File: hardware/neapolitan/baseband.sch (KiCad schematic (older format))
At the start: 136 parts, among them P14 XCVR_CLKOUT, P15 INTR, P16 CLKIN, P18 OEB, P2 CLKOUT, P36 VAA, P37 SCL, P38 SDA, P39 SSP1_SCK, P40 SSP1_MOSI, P41 SSP1_MISO, P53 CS_XCVR, P54 CS_AD, P55 TXENABLE, P56 RXENABLE, P57 XTAL2, P58 GCK1, P59 GCK2, P60 SGPIO_CLK, P61 DA0, P62 DA7, P63 DD0, P64 DD9, P65 DA4, P66 DD5, P67 RSSI, P83 GND, P84 GND, P85 GND, P86 GND, P87 GND, P88 GND, P89 GND, P9 BASEBAND, P90 GND, P91 GND, P92 GND, Q3 MOSFET_P, T3 RX_BALUN, T4 TX_BALUN, U17 MAX2837, U18 MAX5864, U19 SI5351C, X1 GSG-XTAL4PIN

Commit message: Neapolitan: deleted MCU and other things not needed
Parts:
- removed C100, C97, C98: 330nF, hackrf:GSG-0402, symbol C
- removed C101, C103, C107, C108, C109, C110, C95, C96: 22pF, hackrf:GSG-0402, symbol C
- removed C123, C71, C73, C75, C77, C79, C81, C83: 100nF, hackrf:GSG-0402, symbol C
- removed C124, C72, C74, C76, C78, C80, C82: 2.2uF, hackrf:GSG-0402, symbol C
- removed P54: CS_AD, hackrf:GSG-TESTPOINT-50MIL, symbol CONN_1
- removed P58: GCK1, hackrf:GSG-TESTPOINT-50MIL, symbol CONN_1
- removed P59: GCK2, hackrf:GSG-TESTPOINT-50MIL, symbol CONN_1
- removed P60: SGPIO_CLK, hackrf:GSG-TESTPOINT-50MIL, symbol CONN_1
- removed P61: DA0, hackrf:GSG-TESTPOINT-50MIL, symbol CONN_1
- removed P62: DA7, hackrf:GSG-TESTPOINT-50MIL, symbol CONN_1
- removed P63: DD0, hackrf:GSG-TESTPOINT-50MIL, symbol CONN_1
- removed P64: DD9, hackrf:GSG-TESTPOINT-50MIL, symbol CONN_1
- removed P65: DA4, hackrf:GSG-TESTPOINT-50MIL, symbol CONN_1
- removed P66: DD5, hackrf:GSG-TESTPOINT-50MIL, symbol CONN_1
- removed R10, R13, R8, R9: 1k, hackrf:GSG-0402, symbol R
- removed R14, R15, R16, R17: 4k7, hackrf:GSG-0402, symbol R
- removed R20, R21, R22, R23: 0, hackrf:GSG-0402, symbol R
- removed U18: MAX5864, hackrf:GSG-QFN48-7, symbol MAX5864
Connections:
- net labels removed: COM, CS_AD, DA0, DA1, DA2, DA3, DA4, DA5, DA6, DA7, DD0, DD1, DD2, DD3, DD4, DD5, DD6, DD7, DD8, DD9, IA+, IA-, ID+, ID-, QA+, QA-, QD+, QD-, REFN, REFP
- wire segments 320 -> 215
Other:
- note removed: "1%"

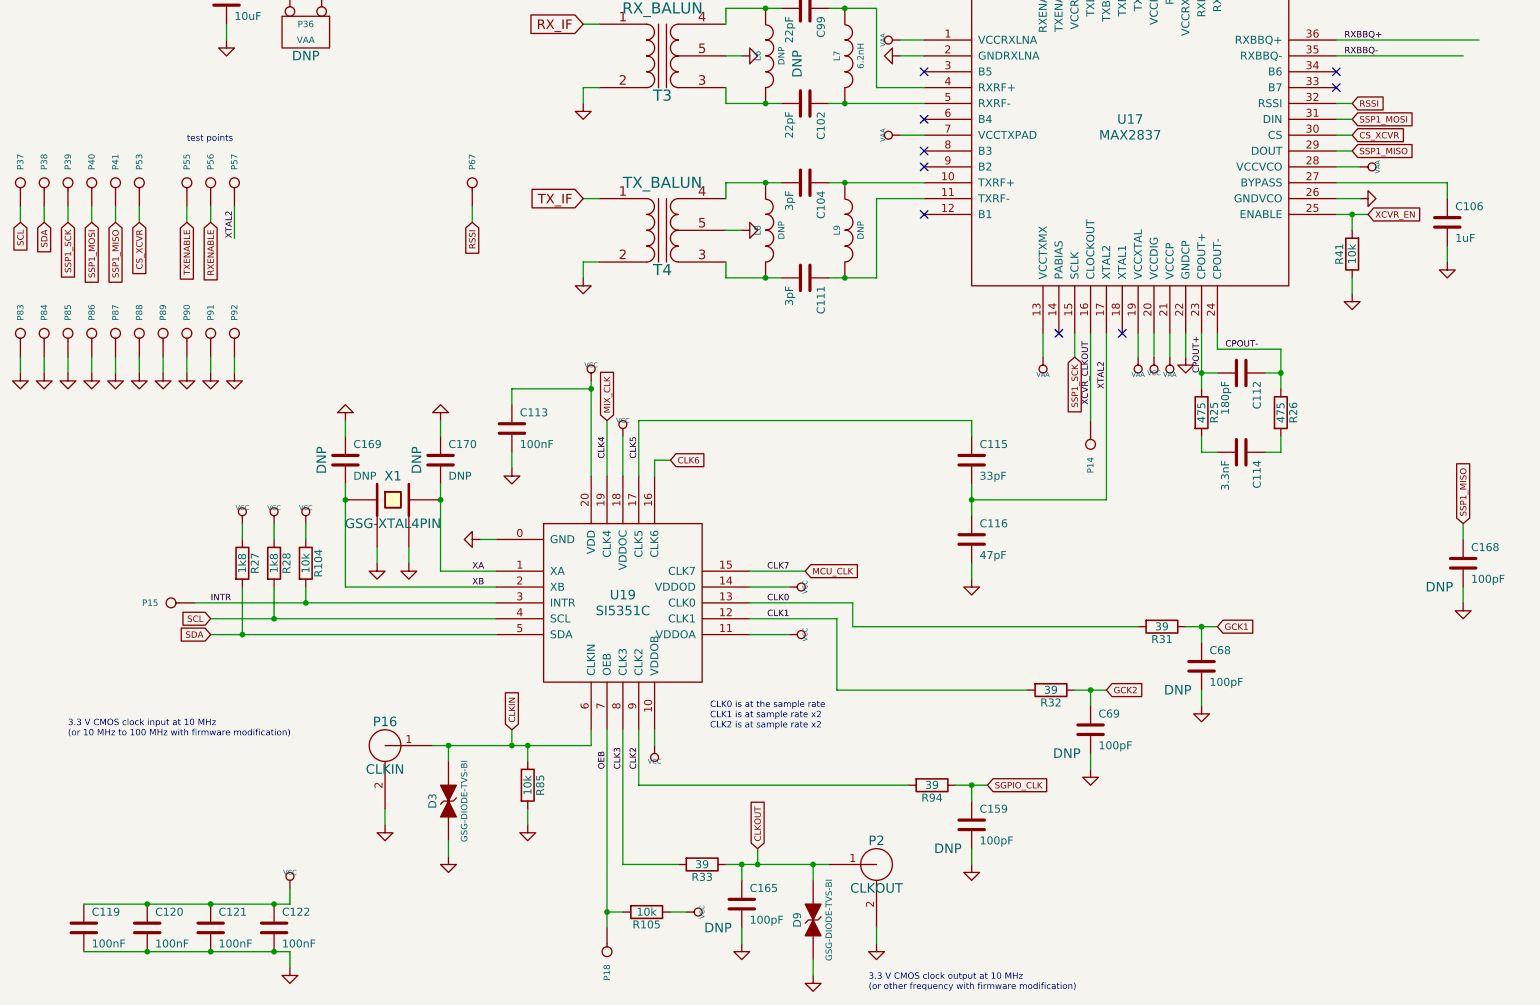
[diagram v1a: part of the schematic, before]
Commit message: Neapolitan: header pin assignments
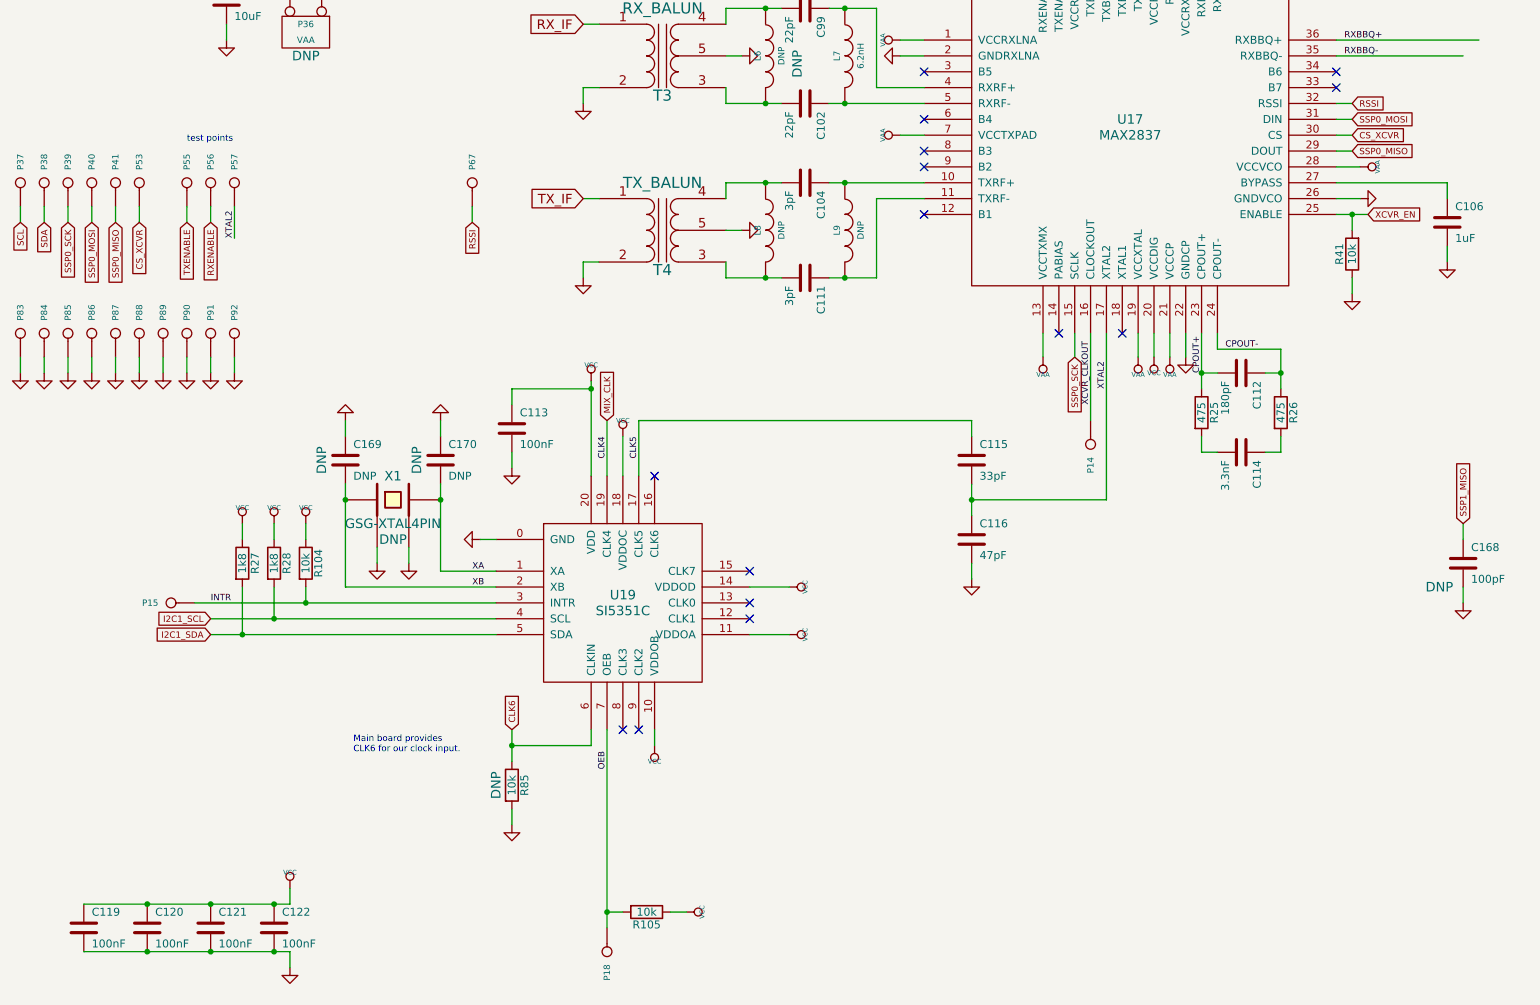
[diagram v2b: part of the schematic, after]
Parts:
- removed C159, C165, C68, C69: 100pF, hackrf:GSG-0402, symbol C
- removed D3, D9: GSG-DIODE-TVS-BI, hackrf:GSG-0402, symbol GSG-DIODE-TVS-BI
- removed P16: CLKIN, hackrf:GSG-SMA-73251-2120, symbol GSG-RF-CONN
- removed P2: CLKOUT, hackrf:GSG-SMA-73251-2120, symbol GSG-RF-CONN
- removed R31, R32, R33, R94: 39, hackrf:GSG-0402, symbol R
- P39: value SSP1_SCK -> SSP0_SCK
- P40: value SSP1_MOSI -> SSP0_MOSI
- P41: value SSP1_MISO -> SSP0_MISO
- R85, X1: Note (none) -> DNP
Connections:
- net labels added: I2C1_SCL, I2C1_SDA, SSP0_MISO, SSP0_MOSI, SSP0_SCK
- net labels removed: CLK0, CLK1, CLK2, CLK3, CLK7, CLKIN, CLKOUT, GCK1, GCK2, MCU_CLK, SGPIO_CLK, SSP1_MOSI, SSP1_SCK
- wire segments 215 -> 182
- no-connect marks 10 -> 16
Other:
- note added: "Main board provides\nCLK6 for our clock input."
- note removed: "3.3 V CMOS clock input at 10 MHz\n(or 10 MHz to 100 MHz with firmware modification)"
- note removed: "3.3 V CMOS clock output at 10 MHz\n(or other frequency with firmware modification)"
- note removed: "CLK0 is at the sample rate\nCLK1 is at sample rate x2\nCLK2 is at sample rate x2"
- moved on the sheet: R85

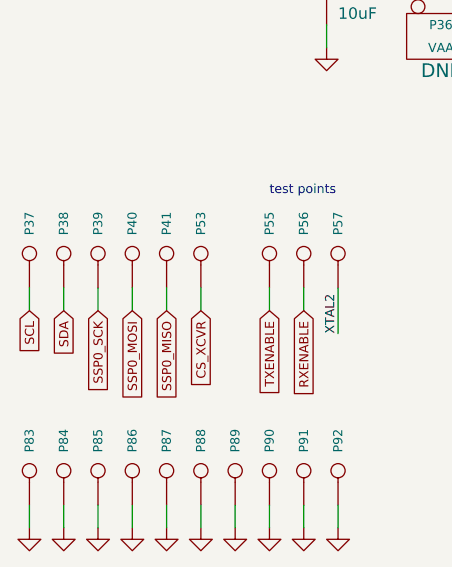
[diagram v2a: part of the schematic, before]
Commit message: Neapolitan: added I/O expander
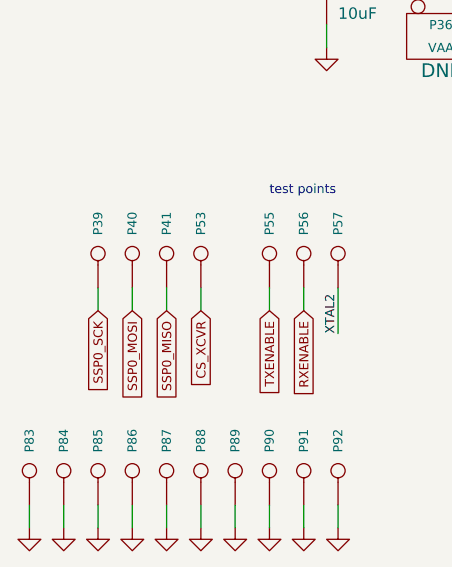
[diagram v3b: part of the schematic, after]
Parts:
- removed P37: SCL, hackrf:GSG-TESTPOINT-50MIL, symbol CONN_1
- removed P38: SDA, hackrf:GSG-TESTPOINT-50MIL, symbol CONN_1
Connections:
- net labels removed: SCL, SDA
- wire segments 182 -> 180
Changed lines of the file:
@@
 LIBS:valves
 LIBS:hackrf
+LIBS:gsg-symbols
 LIBS:neapolitan-cache
 EELAYER 25 0
@@
 F 4 "DNP" H 1000 5300 60  0001 C CNN "Note"
 	1    1000 5300
-	0    -1   -1   0
-$EndComp
-$Comp
-L CONN_1 P38
-U 1 1 5052A32D
-P 850 5300
-F 0 "P38" H 930 5300 40  0000 L CNN
-F 1 "SDA" H 850 5355 30  0001 C CNN
-F 2 "hackrf:GSG-TESTPOINT-50MIL" H 850 5300 60  0001 C CNN
-F 3 "" H 850 5300 60  0001 C CNN
-F 4 "DNP" H 850 5300 60  0001 C CNN "Note"
-	1    850  5300
-	0    -1   -1   0
-$EndComp
-Text GLabel 850  5550 3    40   Input ~ 0
-SDA
-Text GLabel 700  5550 3    40   Input ~ 0
-SCL
-$Comp
-L CONN_1 P37
-U 1 1 5052A309
-P 700 5300
-F 0 "P37" H 780 5300 40  0000 L CNN
-F 1 "SCL" H 700 5355 30  0001 C CNN
-F 2 "hackrf:GSG-TESTPOINT-50MIL" H 700 5300 60  0001 C CNN
-F 3 "" H 700 5300 60  0001 C CNN
-F 4 "DNP" H 700 5300 60  0001 C CNN "Note"
-	1    700  5300
 	0    -1   -1   0
 $EndComp
@@
 	1000 5450 1000 5550
 Wire Wire Line
-	850  5450 850  5550
-Wire Wire Line
-	700  5450 700  5550
-Wire Wire Line
 	2400 3900 2400 4000

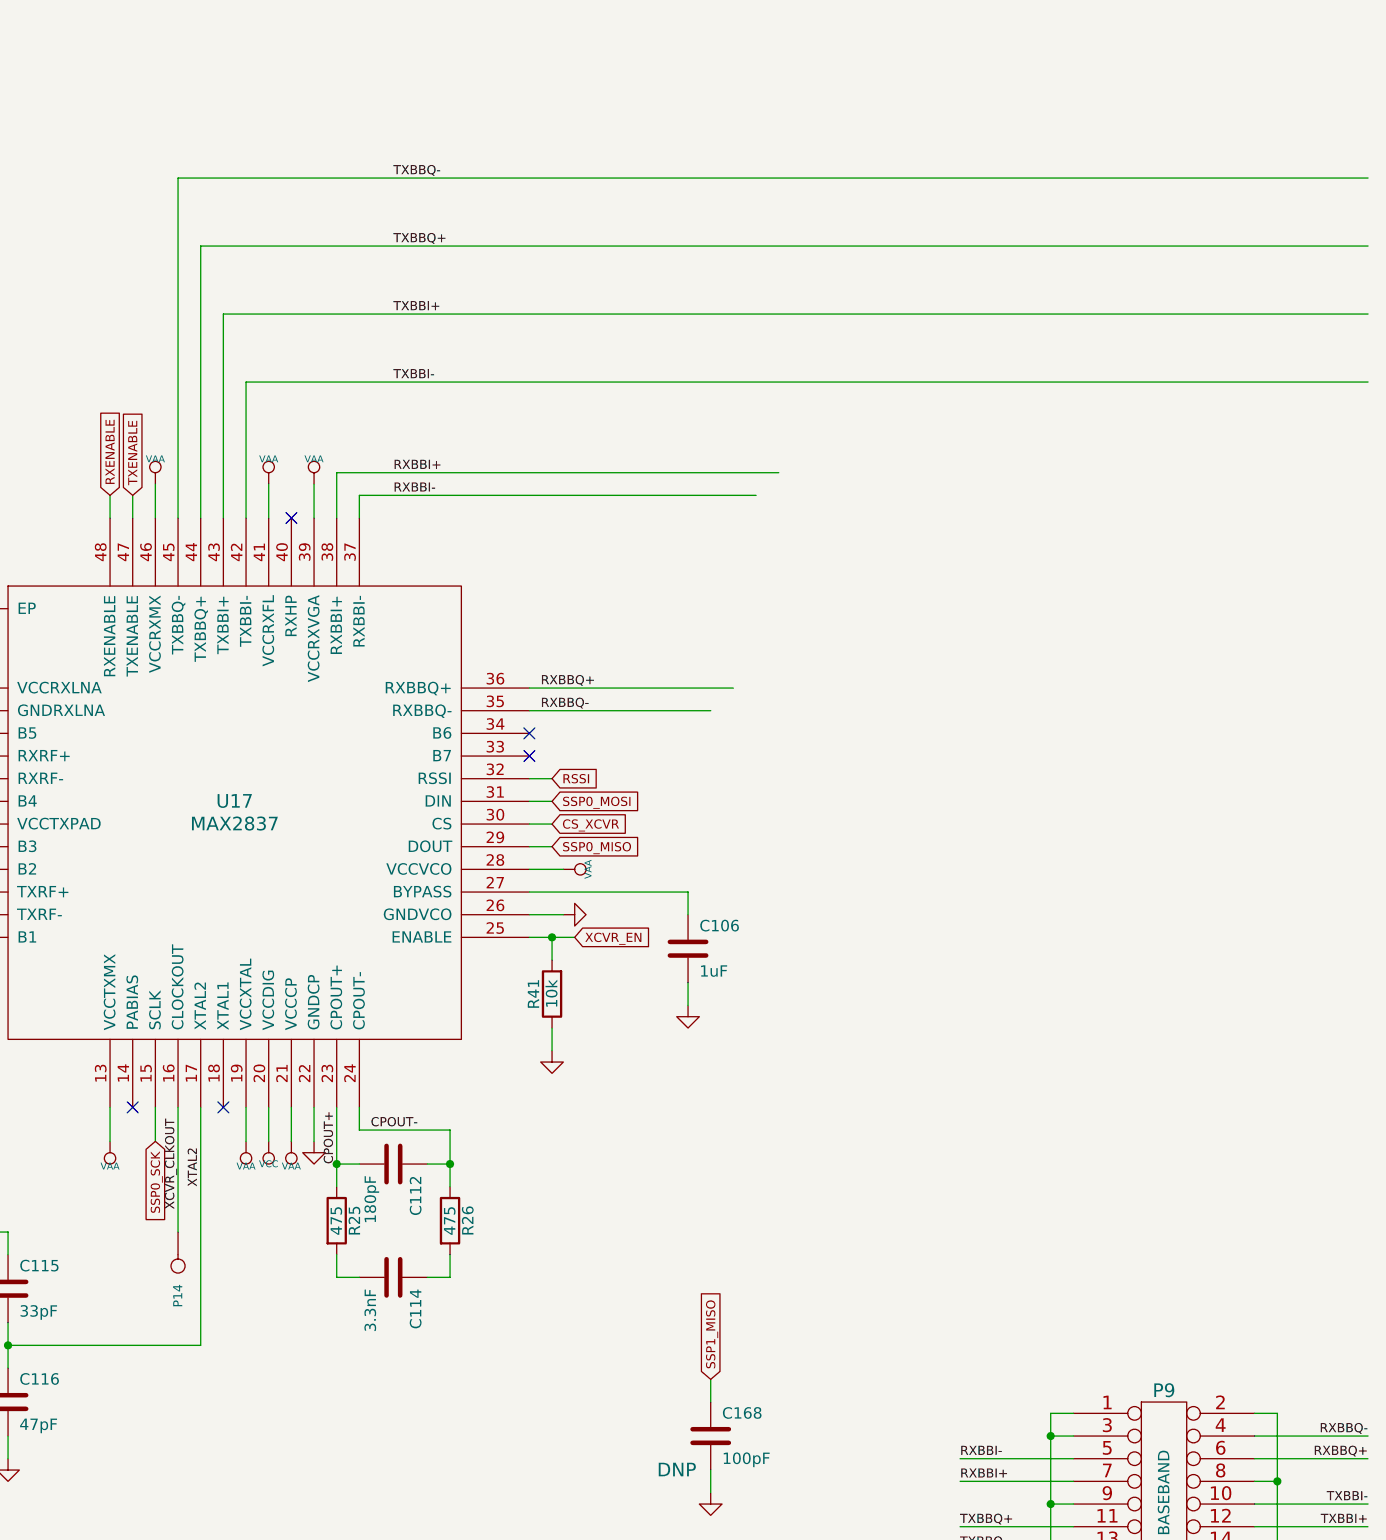
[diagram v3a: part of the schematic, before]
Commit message: Neapolitan: schematic annotation and cleanup
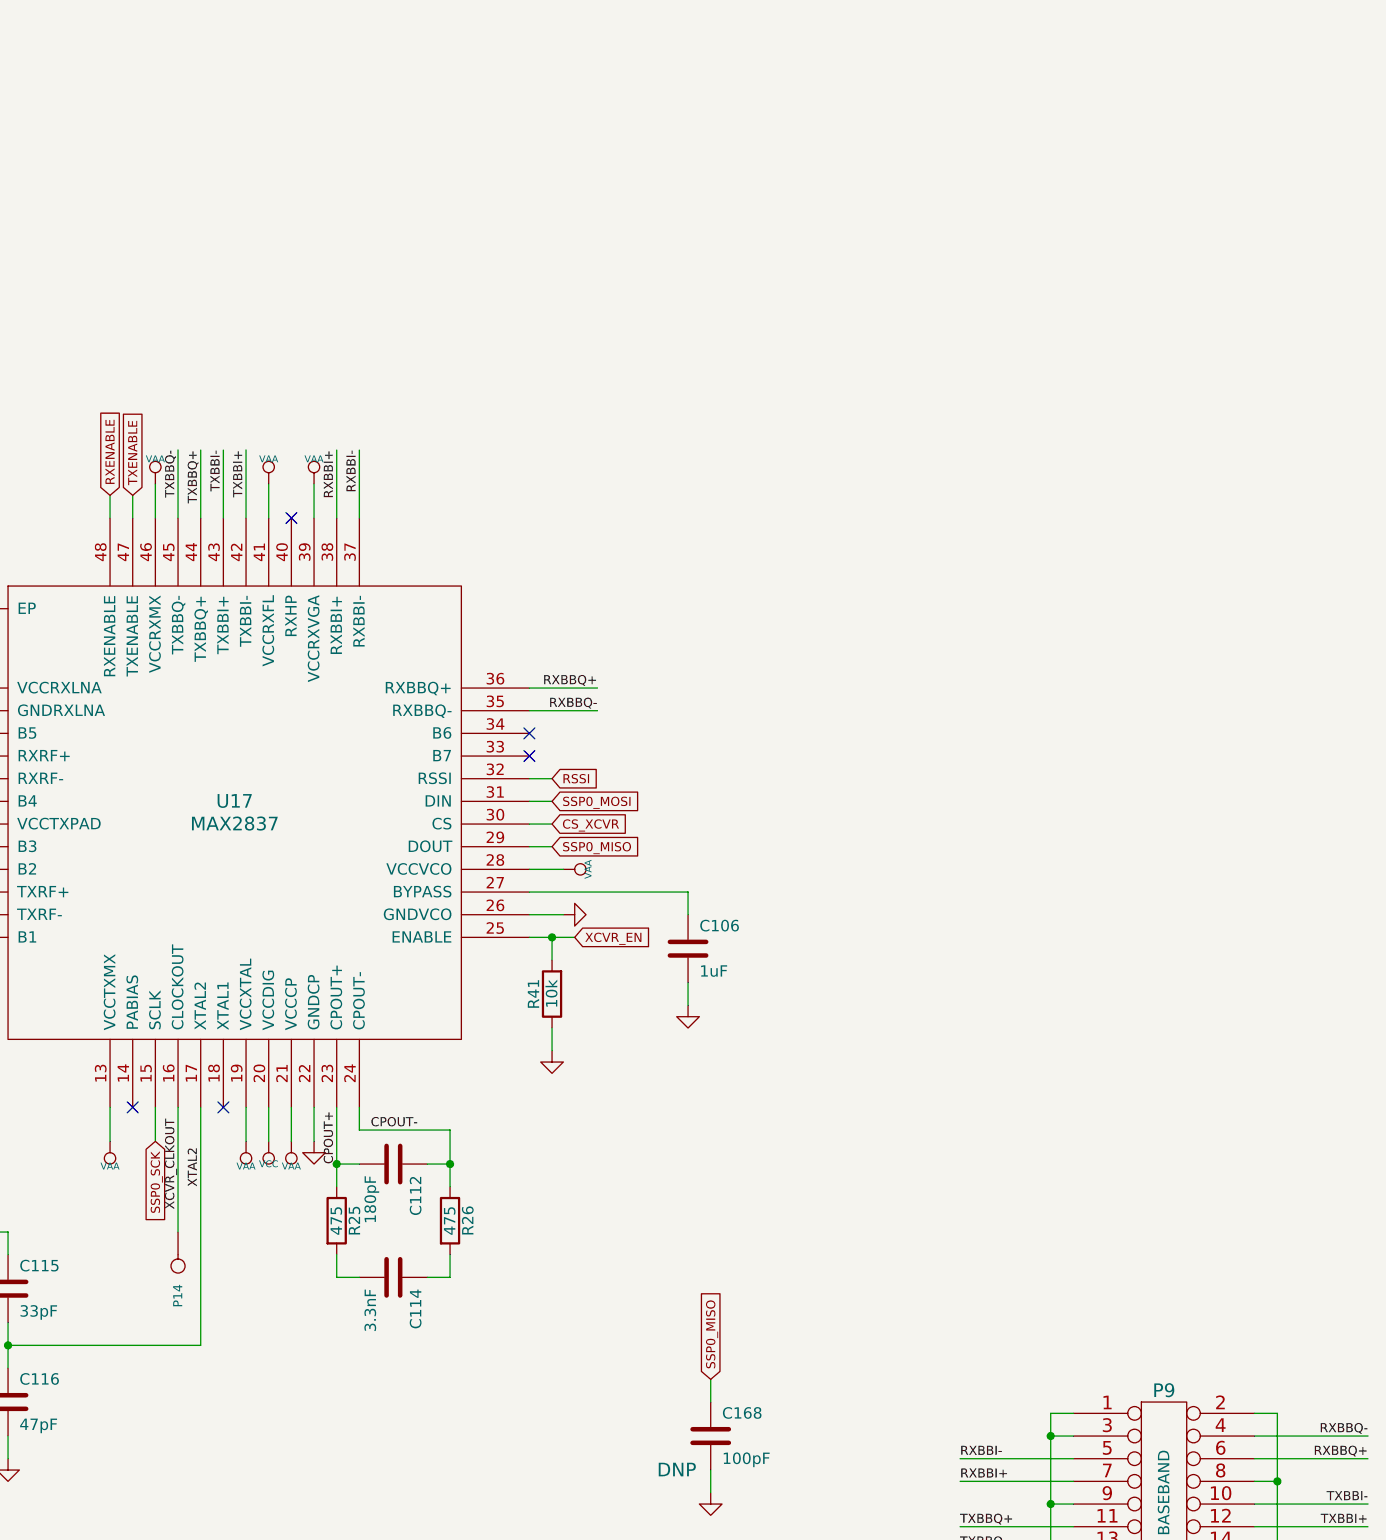
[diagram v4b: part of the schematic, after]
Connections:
- net labels removed: SSP1_MISO
- wire segments 180 -> 174
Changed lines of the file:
@@
 Text Label 1900 7950 0    40   ~ 0
 INTR
-Text Label 9050 4400 0    40   ~ 0
+Text Label 9300 4400 2    40   ~ 0
 RXBBQ+
-Text Label 9050 4500 0    40   ~ 0
+Text Label 9300 4500 2    40   ~ 0
 RXBBQ-
-Text Label 8400 3550 0    40   ~ 0
+Text Label 8250 3350 3    40   ~ 0
 RXBBI-
-Text Label 8400 3450 0    40   ~ 0
+Text Label 8150 3350 3    40   ~ 0
 RXBBI+
-Text Label 8400 3050 0    40   ~ 0
+Text Label 7650 3350 3    40   ~ 0
 TXBBI-
-Text Label 8400 2750 0    40   ~ 0
+Text Label 7750 3350 3    40   ~ 0
 TXBBI+
-Text Label 8400 2450 0    40   ~ 0
+Text Label 7550 3350 3    40   ~ 0
 TXBBQ+
-Text Label 8400 2150 0    40   ~ 0
+Text Label 7450 3350 3    40   ~ 0
 TXBBQ-
 $Comp
@@
 $EndComp
 Text GLabel 9800 7450 1    40   Input ~ 0
-SSP1_MISO
+SSP0_MISO
 $Comp
 L C C168
@@
 	9000 5500 9200 5500
 Wire Wire Line
-	8150 3450 10100 3450
-Wire Wire Line
-	9000 4400 9900 4400
-Wire Wire Line
-	7750 3050 12700 3050
-Wire Wire Line
-	7450 2150 7450 3650
-Wire Wire Line
-	7450 2150 12700 2150
-Wire Wire Line
-	7650 2750 12700 2750
-Wire Wire Line
 	7550 6250 7550 7300
 Wire Wire Line
@@
 	6250 4500 6400 4500
 Wire Wire Line
-	8150 3450 8150 3650
-Wire Wire Line
 	9000 4900 9100 4900
 Wire Wire Line
@@
 Wire Wire Line
 	9000 4800 9100 4800
-Wire Wire Line
-	8250 3550 8250 3650
-Wire Wire Line
-	7650 3650 7650 2750
 Wire Wire Line
 	6250 5000 6400 5000
@@
 Wire Wire Line
 	4300 6550 4300 7150
-Wire Wire Line
-	7750 3650 7750 3050
-Wire Wire Line
-	7550 2450 12700 2450
-Wire Wire Line
-	7550 3650 7550 2450
-Wire Wire Line
-	9000 4500 9800 4500
-Wire Wire Line
-	8250 3550 10000 3550
 Connection ~ 2500 7950
 Wire Wire Line
@@
 NoConn ~ 4500 8750
 NoConn ~ 4600 8750
+Wire Wire Line
+	7450 3350 7450 3650
+Wire Wire Line
+	7550 3650 7550 3350
+Wire Wire Line
+	7650 3350 7650 3650
+Wire Wire Line
+	7750 3350 7750 3650
+Wire Wire Line
+	8250 3350 8250 3650
+Wire Wire Line
+	8150 3650 8150 3350
+Wire Wire Line
+	9300 4400 9000 4400
+Wire Wire Line
+	9000 4500 9300 4500
 $EndSCHEMATC
